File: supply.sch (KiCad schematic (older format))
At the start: 38 parts, among them J1 MJ-3536, J2 2, J3 3, J4 1, J5 GND, J6 Conn_01x01_Female, J7 Conn_01x01_Female, J8 Conn_01x01_Female, J9 Conn_01x01_Female, SW1 TE6-1A-DC-1-PB, U1 LM5157, U2 NE5534

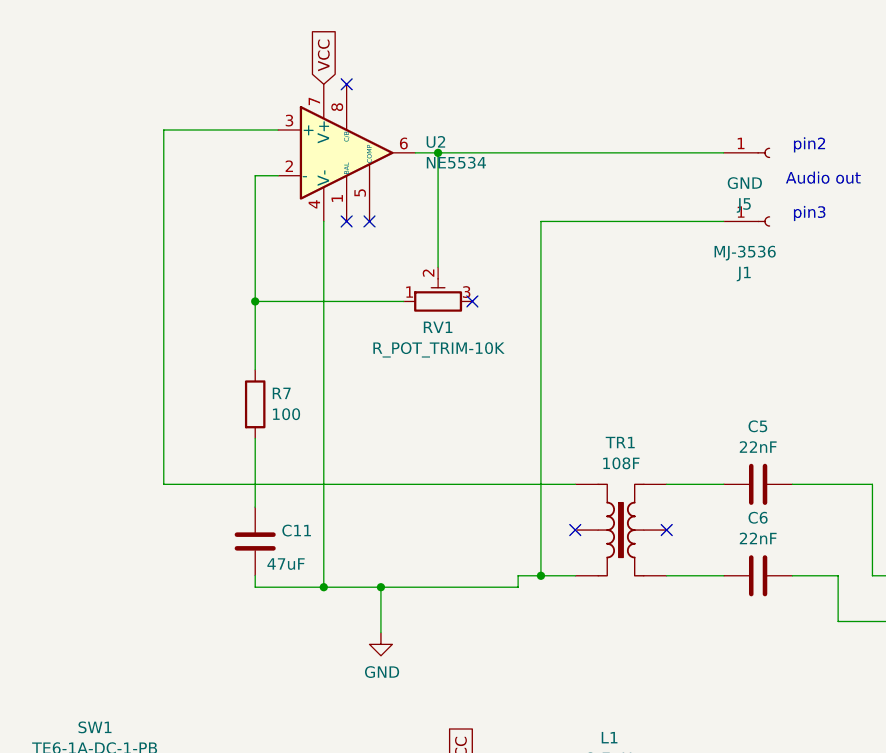
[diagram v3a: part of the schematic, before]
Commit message: Add files via upload
update due to component change.
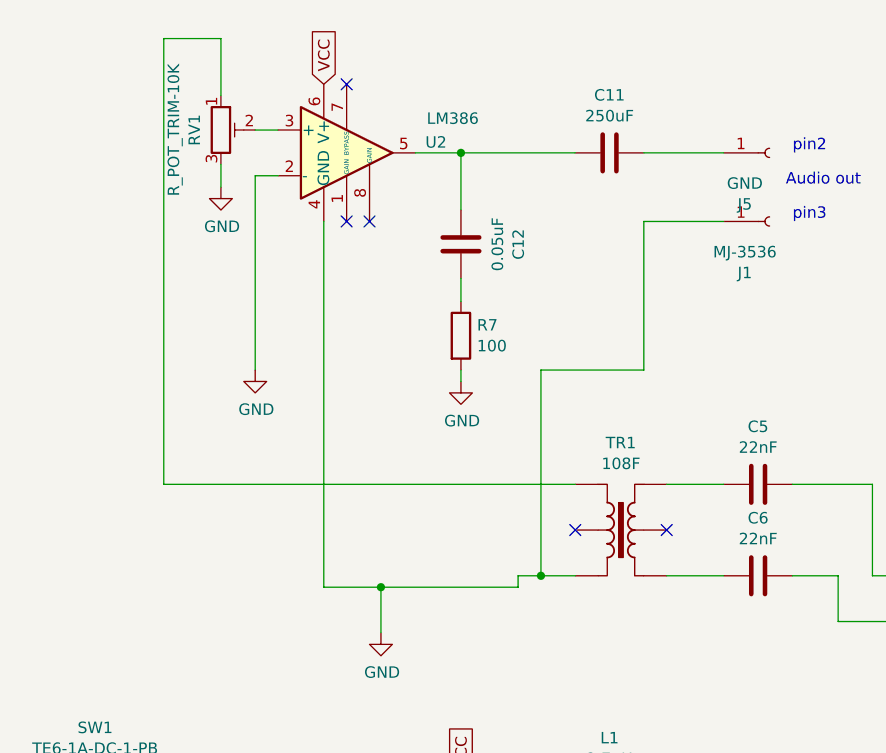
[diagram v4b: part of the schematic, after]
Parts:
- removed U2: NE5534, Package_DIP:DIP-8_W7.62mm_Socket, symbol Amplifier_Operational:NE5534
- added C12: 0.05uF, Capacitor_THT:C_Disc_D3.8mm_W2.6mm_P2.50mm, symbol Device:C
- added U2: LM386, Package_DIP:DIP-8_W7.62mm, symbol Amplifier_Audio:LM386
- C11: value 47uF -> 250uF
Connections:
- net GND: now also R7.2, RV1.3, U2.2 (-), U2.4 (GND); no longer C11.2
- net VCC: now also U2.6 (V+)
- net at TR1.1: now also RV1.1
- net at J5.1 (Pin_1): now also C11.1; no longer RV1.2
- net at R7.1: now also C12.1; no longer RV1.1
- new net: RV1.2, U2.3 (+)
- new net: C11.2, C12.2, U2.5
- no-connect marks 8 -> 7
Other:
- moved on the sheet: RV1
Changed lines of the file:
@@
 Wire Wire Line
 	4800 2900 5050 2900
-Wire Wire Line
-	4150 2900 4250 2900
 NoConn ~ 4400 2700
 NoConn ~ 4800 2700
@@
 Wire Wire Line
 	3550 3150 3550 2950
-Wire Wire Line
-	5050 1350 4250 1350
 $Comp
 L Connector:Conn_01x01_Female J1
@@
 Text Notes 5500 1350 2    50   ~ 0
 pin3
-$Comp
-L Amplifier_Operational:NE5534 U2
-U 1 1 60D1700B
-P 3400 1050
-F 0 "U2" H 3744 1096 50  0000 L CNN
-F 1 "NE5534" H 3744 1005 50  0000 L CNN
-F 2 "Package_DIP:DIP-8_W7.62mm_Socket" H 3450 1100 50  0001 C CNN
-F 3 "http://www.ti.com/lit/ds/symlink/ne5534.pdf" H 3450 1200 50  0001 C CNN
-	1    3400 1050
-	1    0    0    -1
-$EndComp
-Wire Wire Line
-	3100 950  2600 950
-Wire Wire Line
-	2600 950  2600 2500
 Wire Wire Line
 	2600 2500 4400 2500
-$Comp
-L Device:C C11
-U 1 1 60D41FD2
-P 3000 2750
-F 0 "C11" H 3115 2796 50  0000 L CNN
-F 1 "47uF" H 3050 2650 50  0000 L CNN
-F 2 "Capacitor_THT:C_Disc_D3.8mm_W2.6mm_P2.50mm" H 3038 2600 50  0001 C CNN
-F 3 "~" H 3000 2750 50  0001 C CNN
-	1    3000 2750
-	1    0    0    -1
-$EndComp
-$Comp
-L Device:R R7
-U 1 1 60D45884
-P 3000 2150
-F 0 "R7" H 3070 2196 50  0000 L CNN
-F 1 "100" H 3070 2105 50  0000 L CNN
-F 2 "Resistor_THT:R_Axial_DIN0207_L6.3mm_D2.5mm_P7.62mm_Horizontal" V 2930 2150 50  0001 C CNN
-F 3 "~" H 3000 2150 50  0001 C CNN
-	1    3000 2150
-	1    0    0    -1
-$EndComp
 Wire Wire Line
 	3550 2950 3300 2950
-Wire Wire Line
-	3000 2950 3000 2900
 Connection ~ 3550 2950
-Wire Wire Line
-	3000 2000 3000 1700
 Wire Wire Line
 	3000 1150 3100 1150
@@
 L Device:R_POT_TRIM RV1
 U 1 1 60D5425C
-P 3800 1700
-F 0 "RV1" V 3685 1700 50  0000 C CNN
-F 1 "R_POT_TRIM-10K" V 3594 1700 50  0000 C CNN
-F 2 "Connector_PinHeader_2.54mm:PinHeader_1x03_P2.54mm_Vertical" H 3800 1700 50  0001 C CNN
-F 3 "~" H 3800 1700 50  0001 C CNN
-	1    3800 1700
-	0    -1   -1   0
+P 2850 950
+F 0 "RV1" V 2735 950 50  0000 C CNN
+F 1 "R_POT_TRIM-10K" V 2644 950 50  0000 C CNN
+F 2 "Connector_PinHeader_2.54mm:PinHeader_1x03_P2.54mm_Vertical" H 2850 950 50  0001 C CNN
+F 3 "~" H 2850 950 50  0001 C CNN
+	1    2850 950
+	1    0    0    -1
 $EndComp
 Wire Wire Line
 	3300 1350 3300 2950
-Connection ~ 3300 2950
-Wire Wire Line
-	3300 2950 3000 2950
-Wire Wire Line
-	3000 2300 3000 2600
-Wire Wire Line
-	4250 1350 4250 2900
-Connection ~ 4250 2900
-Wire Wire Line
-	4250 2900 4400 2900
-Wire Wire Line
-	3650 1700 3000 1700
-Connection ~ 3000 1700
-Wire Wire Line
-	3000 1700 3000 1150
-Wire Wire Line
-	3800 1550 3800 1050
-Wire Wire Line
-	3800 1050 3700 1050
-Wire Wire Line
-	3800 1050 5050 1050
-Connection ~ 3800 1050
-NoConn ~ 3950 1700
 Text GLabel 3900 3800 1    50   Input ~ 0
 VCC
@@
 	1800 7050 1800 6900
 Connection ~ 1800 6900
+$Comp
+L Amplifier_Audio:LM386 U2
+U 1 1 60D34ED9
+P 3400 1050
+F 0 "U2" H 3744 1096 50  0000 L CNN
+F 1 "LM386" H 3750 1200 50  0000 L CNN
+F 2 "Package_DIP:DIP-8_W7.62mm" H 3500 1150 50  0001 C CNN
+F 3 "http://www.ti.com/lit/ds/symlink/lm386.pdf" H 3600 1250 50  0001 C CNN
+	1    3400 1050
+	1    0    0    -1
+$EndComp
+Wire Wire Line
+	3000 1150 3000 2000
+Wire Wire Line
+	3700 1050 3900 1050
+Wire Wire Line
+	2600 550  2850 550
+Wire Wire Line
+	2850 550  2850 800
+Wire Wire Line
+	2600 550  2600 2500
+Wire Wire Line
+	3000 950  3100 950
+$Comp
+L power:GND #PWR05
+U 1 1 60D4A010
+P 2850 1200
+F 0 "#PWR05" H 2850 950 50  0001 C CNN
+F 1 "GND" H 2855 1027 50  0000 C CNN
+F 2 "" H 2850 1200 50  0001 C CNN
+F 3 "" H 2850 1200 50  0001 C CNN
+	1    2850 1200
+	1    0    0    -1
+$EndComp
+Wire Wire Line
+	2850 1200 2850 1100
+$Comp
+L Device:C C12
+U 1 1 60D50897
+P 3900 1450
+F 0 "C12" V 3648 1450 50  0000 C CNN
+F 1 "0.05uF" V 3739 1450 50  0000 C CNN
+F 2 "Capacitor_THT:C_Disc_D3.8mm_W2.6mm_P2.50mm" H 3938 1300 50  0001 C CNN
+F 3 "~" H 3900 1450 50  0001 C CNN
+	1    3900 1450
+	-1   0    0    1
+$EndComp
+Wire Wire Line
+	4250 2900 4400 2900
+Wire Wire Line
+	4150 2900 4250 2900
+Connection ~ 4250 2900
+Wire Wire Line
+	4700 1350 4700 2000
+Wire Wire Line
+	4700 2000 4250 2000
+Wire Wire Line
+	4700 1350 5050 1350
+Wire Wire Line
+	4250 2000 4250 2900
+$Comp
+L Device:R R7
+U 1 1 60D5806F
+P 3900 1850
+F 0 "R7" H 3970 1896 50  0000 L CNN
+F 1 "100" H 3970 1805 50  0000 L CNN
+F 2 "Resistor_THT:R_Axial_DIN0207_L6.3mm_D2.5mm_P7.62mm_Horizontal" V 3830 1850 50  0001 C CNN
+F 3 "~" H 3900 1850 50  0001 C CNN
+	1    3900 1850
+	1    0    0    -1
+$EndComp
+Wire Wire Line
+	3900 1700 3900 1600
+Wire Wire Line
+	3900 1300 3900 1050
+Connection ~ 3900 1050
+Wire Wire Line
+	3900 1050 4400 1050
+$Comp
+L power:GND #PWR07
+U 1 1 60D62D4D
+P 3900 2050
+F 0 "#PWR07" H 3900 1800 50  0001 C CNN
+F 1 "GND" H 3905 1877 50  0000 C CNN
+F 2 "" H 3900 2050 50  0001 C CNN
+F 3 "" H 3900 2050 50  0001 C CNN
+	1    3900 2050
+	1    0    0    -1
+$EndComp
+Wire Wire Line
+	3900 2050 3900 2000
+$Comp
+L Device:C C11
+U 1 1 60D68843
+P 4550 1050
+F 0 "C11" V 4298 1050 50  0000 C CNN
+F 1 "250uF" V 4389 1050 50  0000 C CNN
+F 2 "Capacitor_THT:C_Disc_D3.8mm_W2.6mm_P2.50mm" H 4588 900 50  0001 C CNN
+F 3 "~" H 4550 1050 50  0001 C CNN
+	1    4550 1050
+	0    1    1    0
+$EndComp
+Wire Wire Line
+	4700 1050 5050 1050
+$Comp
+L power:GND #PWR06
+U 1 1 60D6B86B
+P 3000 2000
+F 0 "#PWR06" H 3000 1750 50  0001 C CNN
+F 1 "GND" H 3005 1827 50  0000 C CNN
+F 2 "" H 3000 2000 50  0001 C CNN
+F 3 "" H 3000 2000 50  0001 C CNN
+	1    3000 2000
+	1    0    0    -1
+$EndComp
 $EndSCHEMATC

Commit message: Add files via upload
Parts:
- removed TR1: 108F, supply:108F, symbol Transformer:TRANSF5
- C11: value 250uF -> 10pF
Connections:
- net GND: now also C6.2
- net at C5.2: now also RV1.1
- no-connect marks 7 -> 5
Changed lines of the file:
@@
 Wire Wire Line
 	1250 4500 1250 5050
-$Comp
-L Transformer:TRANSF5 TR1
-U 1 1 60C979BB
-P 4600 2700
-F 0 "TR1" H 4600 3081 50  0000 C CNN
-F 1 "108F" H 4600 2990 50  0000 C CNN
-F 2 "supply:108F" H 4600 2700 50  0001 C CNN
-F 3 "" H 4600 2700 50  0001 C CNN
-	1    4600 2700
-	1    0    0    -1
-$EndComp
-Wire Wire Line
-	4800 2900 5050 2900
-NoConn ~ 4400 2700
-NoConn ~ 4800 2700
-Wire Wire Line
-	4800 2500 5050 2500
 Wire Wire Line
 	5350 2500 5700 2500
@@
 pin3
 Wire Wire Line
-	2600 2500 4400 2500
-Wire Wire Line
 	3550 2950 3300 2950
 Connection ~ 3550 2950
@@
 $EndComp
 Wire Wire Line
-	4250 2900 4400 2900
-Wire Wire Line
 	4150 2900 4250 2900
 Connection ~ 4250 2900
@@
 P 4550 1050
 F 0 "C11" V 4298 1050 50  0000 C CNN
-F 1 "250uF" V 4389 1050 50  0000 C CNN
+F 1 "10pF" V 4389 1050 50  0000 C CNN
 F 2 "Capacitor_THT:C_Disc_D3.8mm_W2.6mm_P2.50mm" H 4588 900 50  0001 C CNN
 F 3 "~" H 4550 1050 50  0001 C CNN
@@
 	1    0    0    -1
 $EndComp
+Wire Wire Line
+	2600 2500 5050 2500
+Wire Wire Line
+	4250 2900 5050 2900
 $EndSCHEMATC

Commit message: Add files via upload
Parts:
- removed C5, C6: 22nF, Capacitor_THT:C_Disc_D3.8mm_W2.6mm_P2.50mm, symbol Device:C
- removed R4: 6.81K, Resistor_THT:R_Axial_DIN0207_L6.3mm_D2.5mm_P7.62mm_Horizontal, symbol Device:R
- added TR1: 108F, tastatur:108F, symbol Transformer:TRANSF5
- R3: value 6.81K -> 3.3K
- U2: value LM386 -> LM386N-4/NOPB
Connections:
- net GND: now also TR1.3
- net 5: now reaches R3.2
- net 5: now also TR1.5; no longer J2.1 (Pin_1)
- net 4: now reaches J3.1 (Pin_1)
- net 4: now also TR1.4
- net 1: now reaches RV1.1
- net 1: now also TR1.1
- new net 6: J2.1 (Pin_1), TR1.6
- no-connect marks 5 -> 6
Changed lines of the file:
@@
 Comment4 ""
 $EndDescr
-$Comp
-L Device:R R3
-U 1 1 60C4F601
-P 6050 3350
-F 0 "R3" V 5843 3350 50  0000 C CNN
-F 1 "6.81K" V 5934 3350 50  0000 C CNN
-F 2 "Resistor_THT:R_Axial_DIN0207_L6.3mm_D2.5mm_P7.62mm_Horizontal" V 5980 3350 50  0001 C CNN
-F 3 "~" H 6050 3350 50  0001 C CNN
-	1    6050 3350
-	0    1    1    0
-$EndComp
-$Comp
-L Device:R R4
-U 1 1 60C51D2E
-P 6500 3350
-F 0 "R4" V 6293 3350 50  0000 C CNN
-F 1 "6.81K" V 6384 3350 50  0000 C CNN
-F 2 "Resistor_THT:R_Axial_DIN0207_L6.3mm_D2.5mm_P7.62mm_Horizontal" V 6430 3350 50  0001 C CNN
-F 3 "~" H 6500 3350 50  0001 C CNN
-	1    6500 3350
-	0    1    1    0
-$EndComp
-Wire Wire Line
-	6650 3350 6650 2800
-Wire Wire Line
-	6650 2800 6350 2800
-Wire Wire Line
-	5900 3350 5900 3100
 Wire Wire Line
 	3550 2950 4150 2950
 Wire Wire Line
 	4150 2950 4150 2900
-Wire Wire Line
-	5550 2900 5550 3100
-Wire Wire Line
-	5550 3100 5900 3100
-Connection ~ 5900 3100
-$Comp
-L Device:C C6
-U 1 1 60C77EFA
-P 5200 2900
-F 0 "C6" V 4948 2900 50  0000 C CNN
-F 1 "22nF" V 5039 2900 50  0000 C CNN
-F 2 "Capacitor_THT:C_Disc_D3.8mm_W2.6mm_P2.50mm" H 5238 2750 50  0001 C CNN
-F 3 "~" H 5200 2900 50  0001 C CNN
-	1    5200 2900
-	0    1    1    0
-$EndComp
-Wire Wire Line
-	5550 2900 5350 2900
-Wire Wire Line
-	5700 2500 5700 2900
-Wire Wire Line
-	5700 2900 6350 2900
-Wire Wire Line
-	6350 2900 6350 2800
-Connection ~ 6350 2800
-Wire Wire Line
-	6350 2800 6250 2800
 $Comp
 L power:GND #PWR02
@@
 Wire Wire Line
 	1250 4500 1250 5050
-Wire Wire Line
-	5350 2500 5700 2500
-$Comp
-L Device:C C5
-U 1 1 60C76CC6
-P 5200 2500
-F 0 "C5" V 4948 2500 50  0000 C CNN
-F 1 "22nF" V 5039 2500 50  0000 C CNN
-F 2 "Capacitor_THT:C_Disc_D3.8mm_W2.6mm_P2.50mm" H 5238 2350 50  0001 C CNN
-F 3 "~" H 5200 2500 50  0001 C CNN
-	1    5200 2500
-	0    1    1    0
-$EndComp
 Text Notes 7150 6750 0    50   ~ 0
 Balanced power supply with mono headphone output jack.
@@
 $EndComp
 Wire Wire Line
-	6250 2300 6250 2800
-Wire Wire Line
 	6550 2500 6550 2300
 Text Notes 5650 1200 2    50   ~ 0
 Audio out
-Wire Wire Line
-	5900 2300 5900 3100
 $Comp
 L Connector:Conn_01x01_Female J6
@@
 	1    0    0    -1
 $EndComp
-Wire Wire Line
-	6200 3350 6250 3350
 $Comp
 L supply-rescue:LM5157-Keyboard U1
@@
 	6250 3650 6250 3350
 Connection ~ 8500 4200
-Connection ~ 6250 3350
-Wire Wire Line
-	6250 3350 6350 3350
 $Comp
 L Switch:SW_SPST SW1
@@
 U 1 1 60D34ED9
 P 3400 1050
-F 0 "U2" H 3744 1096 50  0000 L CNN
-F 1 "LM386" H 3750 1200 50  0000 L CNN
+F 0 "U2" H 3550 1000 50  0000 L CNN
+F 1 "LM386N-4/NOPB" H 3450 1200 50  0000 L CNN
 F 2 "Package_DIP:DIP-8_W7.62mm" H 3500 1150 50  0001 C CNN
 F 3 "http://www.ti.com/lit/ds/symlink/lm386.pdf" H 3600 1250 50  0001 C CNN
@@
 $EndComp
 Wire Wire Line
-	2600 2500 5050 2500
-Wire Wire Line
-	4250 2900 5050 2900
+	2600 2500 4550 2500
+Wire Wire Line
+	4250 2900 4550 2900
+$Comp
+L Device:R R3
+U 1 1 60D3C3AC
+P 5800 2700
+F 0 "R3" V 5800 2700 50  0000 C CNN
+F 1 "3.3K" V 5684 2700 50  0000 C CNN
+F 2 "Resistor_THT:R_Axial_DIN0207_L6.3mm_D2.5mm_P7.62mm_Horizontal" V 5730 2700 50  0001 C CNN
+F 3 "~" H 5800 2700 50  0001 C CNN
+	1    5800 2700
+	0    1    1    0
+$EndComp
+Wire Wire Line
+	5950 3350 5950 2700
+Wire Wire Line
+	5950 3350 6250 3350
+Wire Wire Line
+	6250 2300 6250 2900
+Wire Wire Line
+	5900 2500 5900 2300
+$Comp
+L Transformer:TRANSF5 TR1
+U 1 1 60D6EE08
+P 4750 2700
+F 0 "TR1" H 4750 3081 50  0000 C CNN
+F 1 "108F" H 4750 2990 50  0000 C CNN
+F 2 "tastatur:108F" H 4750 2700 50  0001 C CNN
+F 3 "" H 4750 2700 50  0001 C CNN
+	1    4750 2700
+	1    0    0    -1
+$EndComp
+Wire Wire Line
+	4950 2500 5900 2500
+Wire Wire Line
+	4950 2900 6250 2900
+Wire Wire Line
+	4950 2700 5650 2700
+NoConn ~ 4550 2700
+Text Label 4500 2500 0    50   ~ 0
+1
+Text Label 4500 2900 0    50   ~ 0
+3
+Text Label 4950 2500 0    50   ~ 0
+6
+Text Label 4950 2900 0    50   ~ 0
+4
+Text Label 4950 2700 0    50   ~ 0
+5
 $EndSCHEMATC
